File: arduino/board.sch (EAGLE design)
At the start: 13 parts

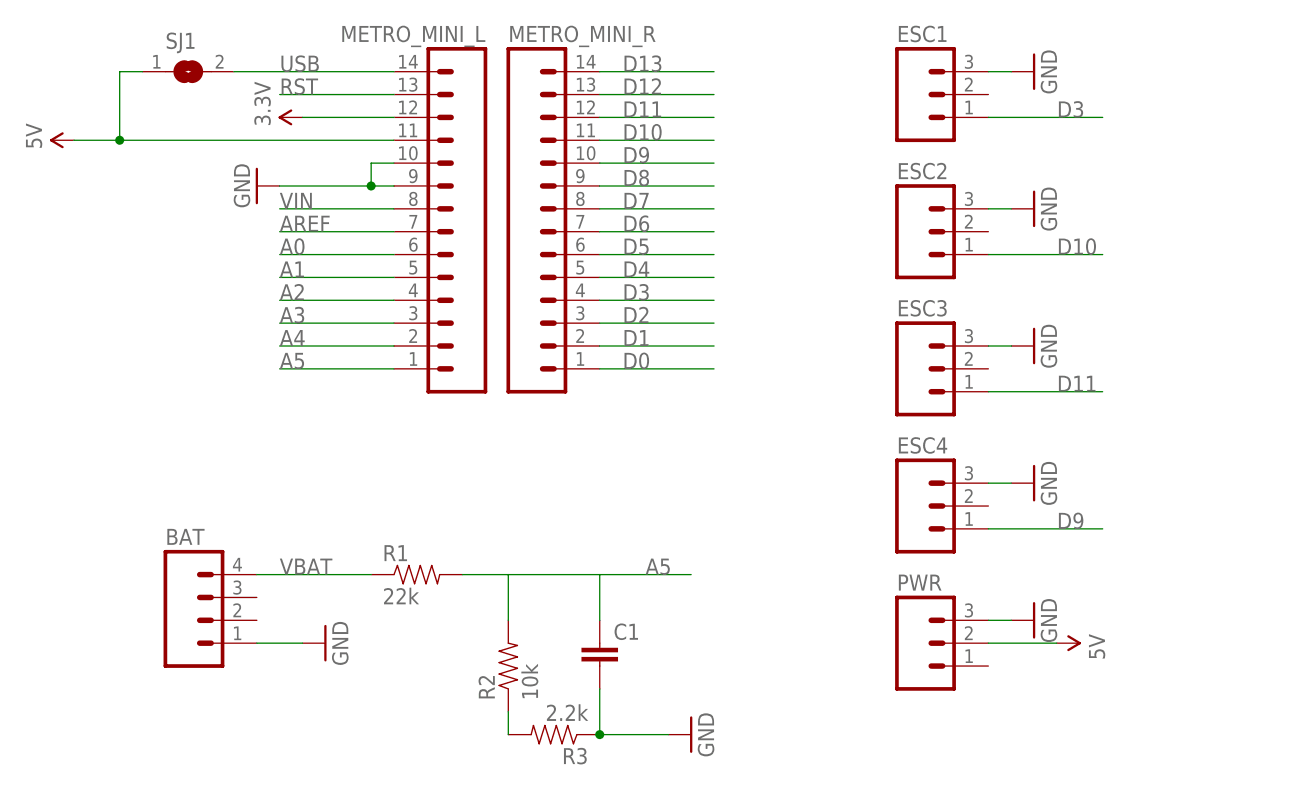
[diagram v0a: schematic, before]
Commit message: Flip board and make ready to build
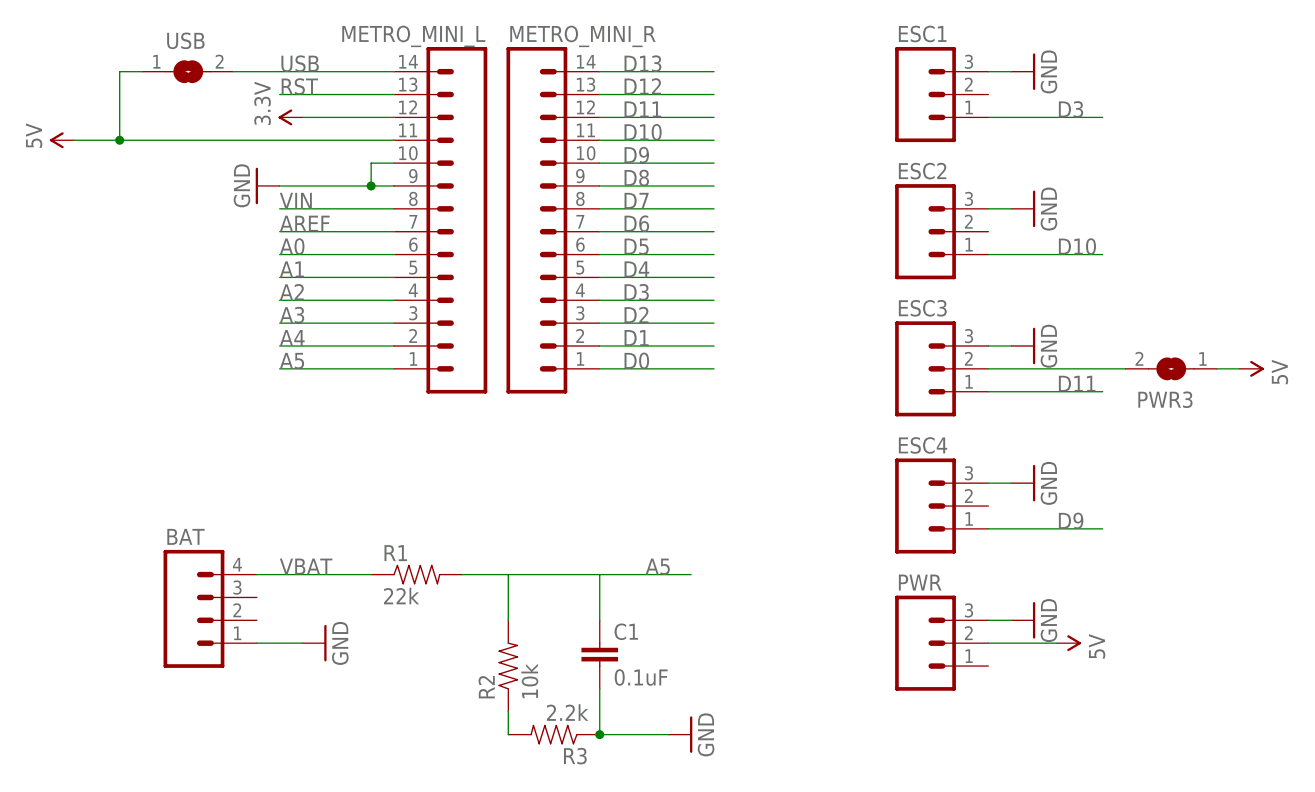
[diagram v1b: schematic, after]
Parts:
- added PWR3: (no value), jumper:SJW
- C1: value (none) -> 0.1uF
- renumbered SJ1 to USB
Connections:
- new net N$2: ESC3.2, PWR3.2
- net 5V: now also PWR3.1
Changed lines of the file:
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@@
 <grid distance="0.1" unitdist="inch" unit="inch" style="lines" multiple="1" display="no" altdistance="0.01" altunitdist="inch" altunit="inch"/>
 <layers>
-<layer number="1" name="Top" color="4" fill="1" visible="no" active="no"/>
-<layer number="16" name="Bottom" color="1" fill="1" visible="no" active="no"/>
-<layer number="17" name="Pads" color="2" fill="1" visible="no" active="no"/>
-<layer number="18" name="Vias" color="2" fill="1" visible="no" active="no"/>
-<layer number="19" name="Unrouted" color="6" fill="1" visible="no" active="no"/>
-<layer number="20" name="Dimension" color="15" fill="1" visible="no" active="no"/>
-<layer number="21" name="tPlace" color="7" fill="1" visible="no" active="no"/>
-<layer number="22" name="bPlace" color="7" fill="1" visible="no" active="no"/>
-<layer number="23" name="tOrigins" color="15" fill="1" visible="no" active="no"/>
-<layer number="24" name="bOrigins" color="15" fill="1" visible="no" active="no"/>
-<layer number="25" name="tNames" color="7" fill="1" visible="no" active="no"/>
-<layer number="26" name="bNames" color="7" fill="1" visible="no" active="no"/>
-<layer number="27" name="tValues" color="7" fill="1" visible="no" active="no"/>
-<layer number="28" name="bValues" color="7" fill="1" visible="no" active="no"/>
+<layer number="1" name="Top" color="4" fill="1" visible="yes" active="no"/>
+<layer number="16" name="Bottom" color="1" fill="1" visible="yes" active="no"/>
+<layer number="17" name="Pads" color="2" fill="1" visible="yes" active="no"/>
+<layer number="18" name="Vias" color="2" fill="1" visible="yes" active="no"/>
+<layer number="19" name="Unrouted" color="6" fill="1" visible="yes" active="no"/>
+<layer number="20" name="Dimension" color="15" fill="1" visible="yes" active="no"/>
+<layer number="21" name="tPlace" color="7" fill="1" visible="yes" active="no"/>
+<layer number="22" name="bPlace" color="7" fill="1" visible="yes" active="no"/>
+<layer number="23" name="tOrigins" color="15" fill="1" visible="yes" active="no"/>
+<layer number="24" name="bOrigins" color="15" fill="1" visible="yes" active="no"/>
+<layer number="25" name="tNames" color="7" fill="1" visible="yes" active="no"/>
+<layer number="26" name="bNames" color="7" fill="1" visible="yes" active="no"/>
+<layer number="27" name="tValues" color="7" fill="1" visible="yes" active="no"/>
+<layer number="28" name="bValues" color="7" fill="1" visible="yes" active="no"/>
 <layer number="29" name="tStop" color="7" fill="3" visible="no" active="no"/>
 <layer number="30" name="bStop" color="7" fill="6" visible="no" active="no"/>
@@
 <layer number="35" name="tGlue" color="7" fill="4" visible="no" active="no"/>
 <layer number="36" name="bGlue" color="7" fill="5" visible="no" active="no"/>
-<layer number="37" name="tTest" color="7" fill="1" visible="no" active="no"/>
-<layer number="38" name="bTest" color="7" fill="1" visible="no" active="no"/>
+<layer number="37" name="tTest" color="7" fill="1" visible="yes" active="no"/>
+<layer number="38" name="bTest" color="7" fill="1" visible="yes" active="no"/>
 <layer number="39" name="tKeepout" color="4" fill="11" visible="no" active="no"/>
 <layer number="40" name="bKeepout" color="1" fill="11" visible="no" active="no"/>
@@
 <layer number="44" name="Drills" color="7" fill="1" visible="no" active="no"/>
 <layer number="45" name="Holes" color="7" fill="1" visible="no" active="no"/>
-<layer number="46" name="Milling" color="3" fill="1" visible="no" active="no"/>
-<layer number="47" name="Measures" color="7" fill="1" visible="no" active="no"/>
-<layer number="48" name="Document" color="7" fill="1" visible="no" active="no"/>
-<layer number="49" name="Reference" color="7" fill="1" visible="no" active="no"/>
-<layer number="50" name="dxf" color="7" fill="1" visible="no" active="no"/>
-<layer number="51" name="tDocu" color="7" fill="1" visible="no" active="no"/>
-<layer number="52" name="bDocu" color="7" fill="1" visible="no" active="no"/>
-<layer number="53" name="tGND_GNDA" color="7" fill="9" visible="no" active="no"/>
-<layer number="54" name="bGND_GNDA" color="1" fill="9" visible="no" active="no"/>
-<layer number="56" name="wert" color="7" fill="1" visible="no" active="no"/>
-<layer number="57" name="tCAD" color="7" fill="1" visible="no" active="no"/>
-<layer number="59" name="tCarbon" color="7" fill="1" visible="no" active="no"/>
-<layer number="60" name="bCarbon" color="7" fill="1" visible="no" active="no"/>
+<layer number="46" name="Milling" color="3" fill="1" visible="yes" active="no"/>
+<layer number="47" name="Measures" color="7" fill="1" visible="yes" active="no"/>
+<layer number="48" name="Document" color="7" fill="1" visible="yes" active="no"/>
+<layer number="49" name="Reference" color="7" fill="1" visible="yes" active="no"/>
+<layer number="50" name="dxf" color="7" fill="1" visible="yes" active="no"/>
+<layer number="51" name="tDocu" color="7" fill="1" visible="yes" active="no"/>
+<layer number="52" name="bDocu" color="7" fill="1" visible="yes" active="no"/>
+<layer number="53" name="tGND_GNDA" color="7" fill="9" visible="yes" active="no"/>
+<layer number="54" name="bGND_GNDA" color="1" fill="9" visible="yes" active="no"/>
+<layer number="56" name="wert" color="7" fill="1" visible="yes" active="no"/>
+<layer number="57" name="tCAD" color="7" fill="1" visible="yes" active="no"/>
+<layer number="59" name="tCarbon" color="7" fill="1" visible="yes" active="no"/>
+<layer number="60" name="bCarbon" color="7" fill="1" visible="yes" active="no"/>
 <layer number="90" name="Modules" color="5" fill="1" visible="yes" active="yes"/>
 <layer number="91" name="Nets" color="2" fill="1" visible="yes" active="yes"/>
@@
 <part name="GND6" library="supply1" deviceset="GND" device=""/>
 <part name="SUPPLY3" library="SparkFun-Aesthetics" deviceset="5V" device=""/>
-<part name="SJ1" library="jumper" deviceset="SJ" device="W"/>
+<part name="USB" library="jumper" deviceset="SJ" device="W"/>
 <part name="GND7" library="supply1" deviceset="GND" device=""/>
 <part name="R1" library="SparkFun-Passives" deviceset="RESISTOR" device="PTH-1/4W" value="22k"/>
 <part name="R2" library="SparkFun-Passives" deviceset="RESISTOR" device="PTH-1/4W" value="10k"/>
-<part name="C1" library="SparkFun-Capacitors" deviceset="CAP" device="_"/>
+<part name="C1" library="SparkFun-Capacitors" deviceset="CAP" device="_" value="0.1uF"/>
 <part name="GND8" library="supply1" deviceset="GND" device=""/>
 <part name="R3" library="SparkFun-Passives" deviceset="RESISTOR" device="PTH-1/4W" value="2.2k"/>
+<part name="FRAME1" library="frames" deviceset="LETTER_L" device=""/>
+<part name="PWR3" library="jumper" deviceset="SJ" device="W"/>
+<part name="SUPPLY4" library="SparkFun-Aesthetics" deviceset="5V" device=""/>
 </parts>
 <sheets>
@@
 <instance part="GND6" gate="1" x="93.98" y="43.18" rot="R90"/>
 <instance part="SUPPLY3" gate="G$1" x="96.52" y="-20.32" rot="R270"/>
-<instance part="SJ1" gate="1" x="0" y="43.18"/>
+<instance part="USB" gate="1" x="0" y="43.18"/>
 <instance part="GND7" gate="1" x="15.24" y="-20.32" rot="R90"/>
 <instance part="R1" gate="G$1" x="25.4" y="-12.7"/>
@@
 <instance part="GND8" gate="1" x="55.88" y="-30.48" rot="R90"/>
 <instance part="R3" gate="G$1" x="40.64" y="-30.48" rot="R180"/>
+<instance part="FRAME1" gate="G$1" x="-76.2" y="-93.98"/>
+<instance part="FRAME1" gate="G$2" x="71.12" y="-93.98"/>
+<instance part="PWR3" gate="1" x="109.22" y="10.16" rot="R180"/>
+<instance part="SUPPLY4" gate="G$1" x="116.84" y="10.16" rot="R270"/>
 </instances>
 <busses>
@@
 <wire x1="22.86" y1="43.18" x2="5.08" y2="43.18" width="0.1524" layer="91"/>
 <label x="10.16" y="43.18" size="1.778" layer="95"/>
-<pinref part="SJ1" gate="1" pin="2"/>
+<pinref part="USB" gate="1" pin="2"/>
 </segment>
 </net>
@@
 <wire x1="22.86" y1="35.56" x2="-7.62" y2="35.56" width="0.1524" layer="91"/>
 <pinref part="SUPPLY1" gate="G$1" pin="5V"/>
-<pinref part="SJ1" gate="1" pin="1"/>
+<pinref part="USB" gate="1" pin="1"/>
 <wire x1="-7.62" y1="35.56" x2="-12.7" y2="35.56" width="0.1524" layer="91"/>
 <wire x1="-5.08" y1="43.18" x2="-7.62" y2="43.18" width="0.1524" layer="91"/>
@@
 <wire x1="96.52" y1="-20.32" x2="88.9" y2="-20.32" width="0.1524" layer="91"/>
 </segment>
+<segment>
+<pinref part="PWR3" gate="1" pin="1"/>
+<pinref part="SUPPLY4" gate="G$1" pin="5V"/>
+<wire x1="116.84" y1="10.16" x2="114.3" y2="10.16" width="0.1524" layer="91"/>
+</segment>
 </net>
 <net name="3.3V" class="0">
@@
 </segment>
 </net>
+<net name="N$2" class="0">
+<segment>
+<pinref part="ESC3" gate="G$1" pin="2"/>
+<pinref part="PWR3" gate="1" pin="2"/>
+<wire x1="104.14" y1="10.16" x2="88.9" y2="10.16" width="0.1524" layer="91"/>
+</segment>
+</net>
